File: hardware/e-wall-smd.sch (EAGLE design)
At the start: 56 parts, among them IC1 74HCT595D, IC2 74HCT595D, IC3 74HCT595D, Q1 2N7002P, Q10 2N7002P, Q11 2N7002P, Q12 2N7002P, Q13 2N7002P, Q14 2N7002P, Q15 2N7002P, Q16 2N7002P, Q17 2N7002P, Q18 2N7002P, Q19 2N7002P, Q2 2N7002P, Q20 2N7002P, Q21 2N7002P, Q22 2N7002P, Q23 2N7002P, Q24 2N7002P, Q3 2N7002P, Q4 2N7002P, Q5 2N7002P, Q6 2N7002P, Q7 2N7002P, Q8 2N7002P, Q9 2N7002P, T1 BC547, T2 BC557, T3 BC547

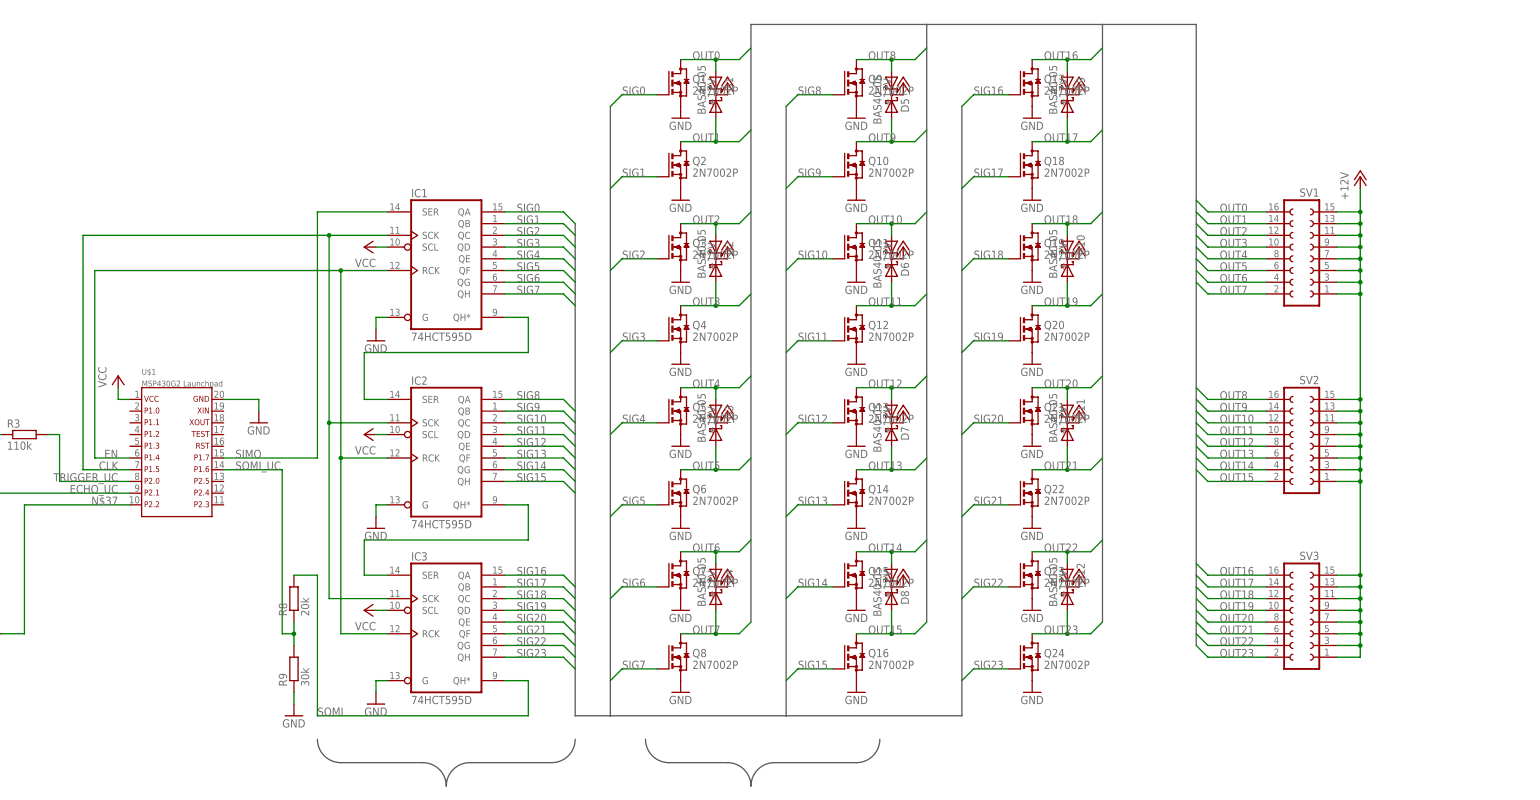
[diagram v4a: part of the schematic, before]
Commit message: Zusätzliches Schieberegister mit Treiber für mehr Strom
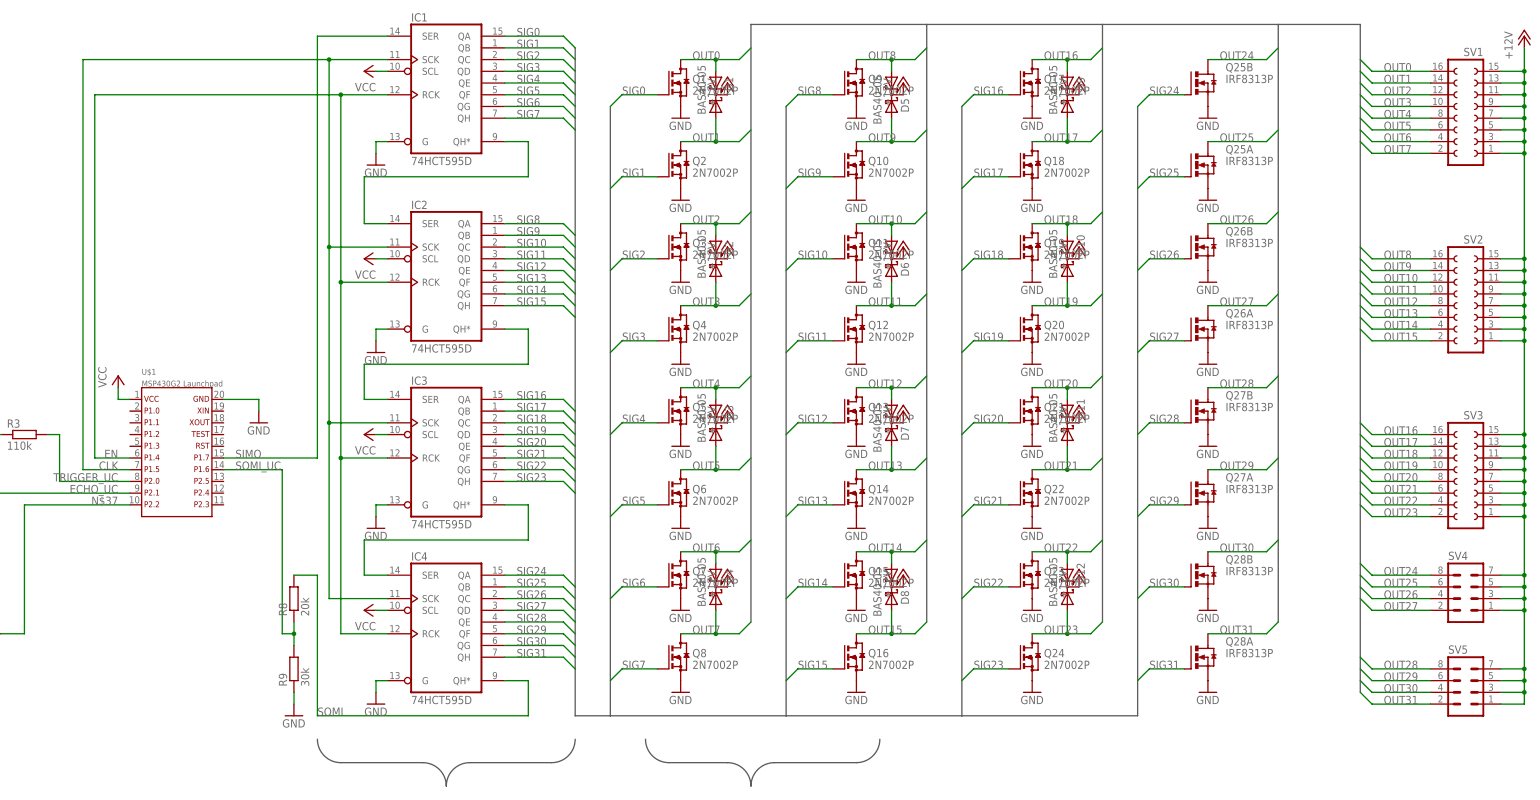
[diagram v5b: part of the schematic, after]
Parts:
- added IC4: 74HCT595D, 74xx-eu:74HCT595D
- added Q25, Q26, Q27, Q28: IRF8313P, transistor-power:IRF8313P
- added SV4, SV5: (no value), con-lstb:MA04-2
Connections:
- new net N$3: IC3A.QH*, IC4A.SER
- new net OUT24: Q25B.D, SV4.8
- new net OUT25: Q25A.D, SV4.6
- new net OUT26: Q26B.D, SV4.4
- new net OUT27: Q26A.D, SV4.2
- new net OUT28: Q27B.D, SV5.8
- new net OUT29: Q27A.D, SV5.6
- new net OUT30: Q28B.D, SV5.4
- new net OUT31: Q28A.D, SV5.2
- new net SIG24: IC4A.QA, Q25B.G
- new net SIG25: IC4A.QB, Q25A.G
- new net SIG26: IC4A.QC, Q26B.G
- new net SIG27: IC4A.QD, Q26A.G
- new net SIG28: IC4A.QE, Q27B.G
- new net SIG29: IC4A.QF, Q27A.G
- new net SIG30: IC4A.QG, Q28B.G
- new net SIG31: IC4A.QH, Q28A.G
- net +12V: now also SV4.1, SV4.3, SV4.5, SV4.7, SV5.1, SV5.3, SV5.5, SV5.7
- net CLK: now also IC4A.SCK
- net EN: now also IC4A.RCK
- net GND: now also IC4A.G, Q25A.S, Q25B.S, Q26A.S, Q26B.S, Q27A.S, Q27B.S, Q28A.S, Q28B.S
- net SOMI: now also IC4A.QH*; no longer IC3A.QH*
- net VCC: now also IC4A.SCL
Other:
- moved on the sheet: IC1, IC2, IC3, SV1, SV2, SV3

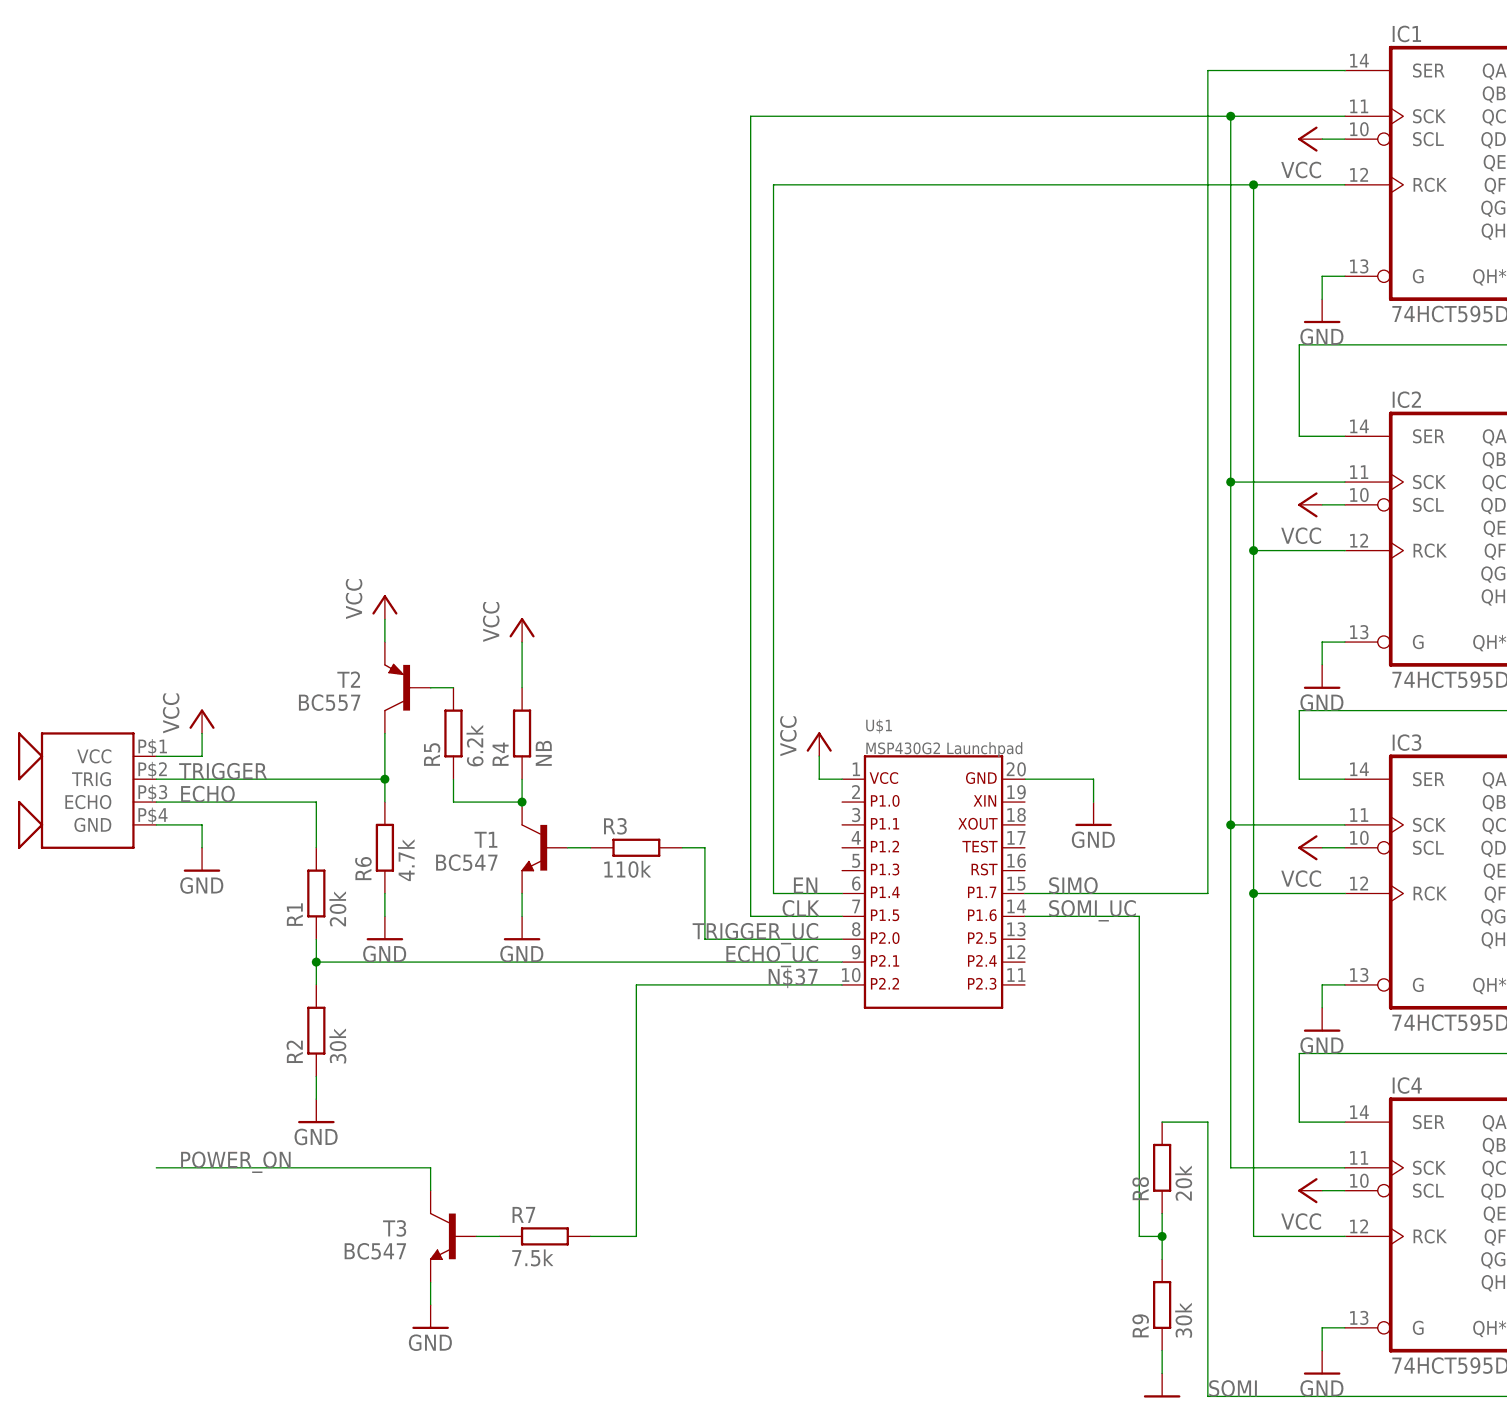
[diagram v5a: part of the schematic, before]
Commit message: Anschlüsse für Versorgung und Kupferflächen für MAsse und 12V
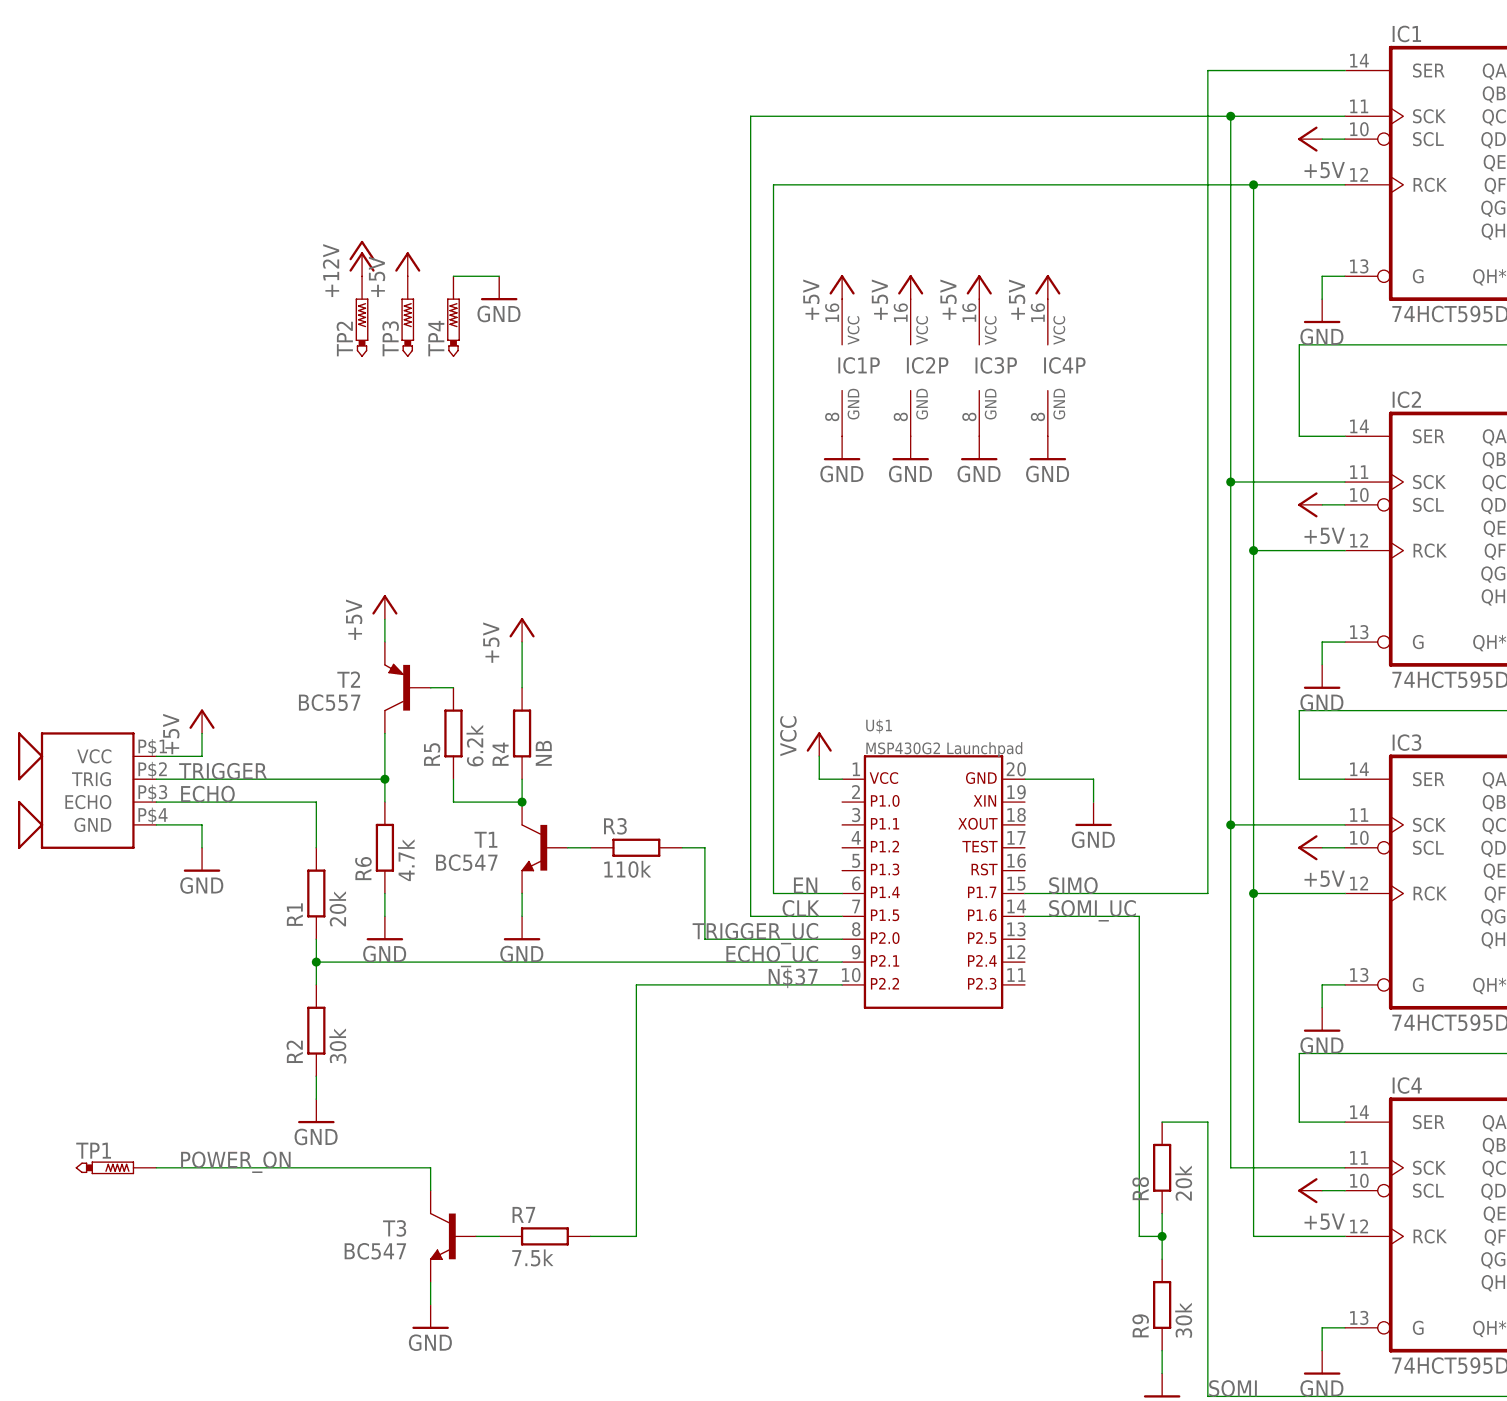
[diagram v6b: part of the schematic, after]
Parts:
- added TP1, TP2, TP3, TP4: PTR1PAD1-20, testpad:PTR1PAD1-20
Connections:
- removed net GND: IC1A.G, IC2A.G, IC3A.G, IC4A.G, Q1.S, Q10.S, Q11.S, Q12.S, Q13.S, Q14.S, Q15.S, Q16.S, Q17.S, Q18.S, Q19.S, Q2.S, Q20.S, Q21.S, Q22.S, Q23.S, Q24.S, Q25A.S, Q25B.S, Q26A.S, Q26B.S, Q27A.S, Q27B.S, Q28A.S, Q28B.S, Q3.S, Q4.S, Q5.S, Q6.S, Q7.S, Q8.S, Q9.S, R2.1, R6.1, R9.1, T1.E, T3.E, U$1.20, U$2.GND
- new net +5V: IC1A.SCL, IC1P.VCC, IC2A.SCL, IC2P.VCC, IC3A.SCL, IC3P.VCC, IC4A.SCL, IC4P.VCC, R4.2, T2.E, TP3.TP, U$2.VCC
- new net CP: IC1A.G, IC1P.GND, IC2A.G, IC2P.GND, IC3A.G, IC3P.GND, IC4A.G, IC4P.GND, Q1.S, Q10.S, Q11.S, Q12.S, Q13.S, Q14.S, Q15.S, Q16.S, Q17.S, Q18.S, Q19.S, Q2.S, Q20.S, Q21.S, Q22.S, Q23.S, Q24.S, Q25A.S, Q25B.S, Q26A.S, Q26B.S, Q27A.S, Q27B.S, Q28A.S, Q28B.S, Q3.S, Q4.S, Q5.S, Q6.S, Q7.S, Q8.S, Q9.S, R2.1, R6.1, R9.1, T1.E, T3.E, TP4.TP, U$1.20, U$2.GND
- net +12V: now also TP2.TP
- net POWER_ON: now also TP1.TP
- net VCC: no longer IC1A.SCL, IC2A.SCL, IC3A.SCL, IC4A.SCL, R4.2, T2.E, U$2.VCC

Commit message: Pegelwandler mit FET
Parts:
- removed R5: 6.2k, resistor:R-EU_R1206
- removed T1, T3: BC547, transistor:-NPN-SOT23-EBC
- removed T2: BC557, transistor:-PNP-SOT23-BCE
- added Q29, Q30: 2N7002P, transistor-small-signal:BSS123
- added Q31: BSS84, transistor-small-signal:BSS84
- R3: value 110k -> 100k
- R4: value NB -> 100k
- R7: value 7.5k -> 100k
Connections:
- removed net CP: IC1A.G, IC1P.GND, IC2A.G, IC2P.GND, IC3A.G, IC3P.GND, IC4A.G, IC4P.GND, Q1.S, Q10.S, Q11.S, Q12.S, Q13.S, Q14.S, Q15.S, Q16.S, Q17.S, Q18.S, Q19.S, Q2.S, Q20.S, Q21.S, Q22.S, Q23.S, Q24.S, Q25A.S, Q25B.S, Q26A.S, Q26B.S, Q27A.S, Q27B.S, Q28A.S, Q28B.S, Q3.S, Q4.S, Q5.S, Q6.S, Q7.S, Q8.S, Q9.S, R2.1, R6.1, R9.1, T1.E, T3.E, TP4.TP, U$1.20, U$2.GND
- removed net N$33: R3.1, T1.B
- removed net N$35: R5.2, T2.B
- removed net N$36: R7.1, T3.B
- new net GND: IC1A.G, IC1P.GND, IC2A.G, IC2P.GND, IC3A.G, IC3P.GND, IC4A.G, IC4P.GND, Q1.S, Q10.S, Q11.S, Q12.S, Q13.S, Q14.S, Q15.S, Q16.S, Q17.S, Q18.S, Q19.S, Q2.S, Q20.S, Q21.S, Q22.S, Q23.S, Q24.S, Q25A.S, Q25B.S, Q26A.S, Q26B.S, Q27A.S, Q27B.S, Q28A.S, Q28B.S, Q29.S, Q3.S, Q30.S, Q4.S, Q5.S, Q6.S, Q7.S, Q8.S, Q9.S, R2.1, R3.1, R6.1, R7.1, R9.1, TP4.TP, U$1.20, U$2.GND
- net +5V: now also Q31.S; no longer T2.E
- net N$34: now also Q30.D, Q31.G; no longer R5.1, T1.C
- net N$37: now also Q29.G
- net POWER_ON: now also Q29.D; no longer T3.C
- net TRIGGER: now also Q31.D; no longer T2.C
- net TRIGGER_UC: now also Q30.G
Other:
- moved on the sheet: R3, R4, R6, R7
